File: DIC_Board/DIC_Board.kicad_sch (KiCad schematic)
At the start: 0 parts

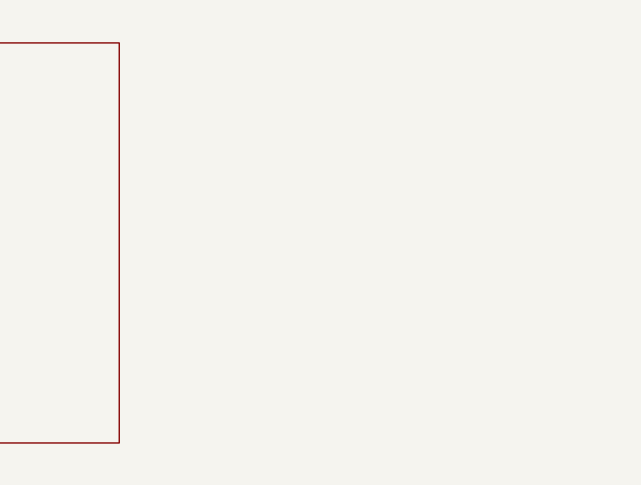
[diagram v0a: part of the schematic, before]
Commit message: Add MCU schematic hierarchy and pin configuration
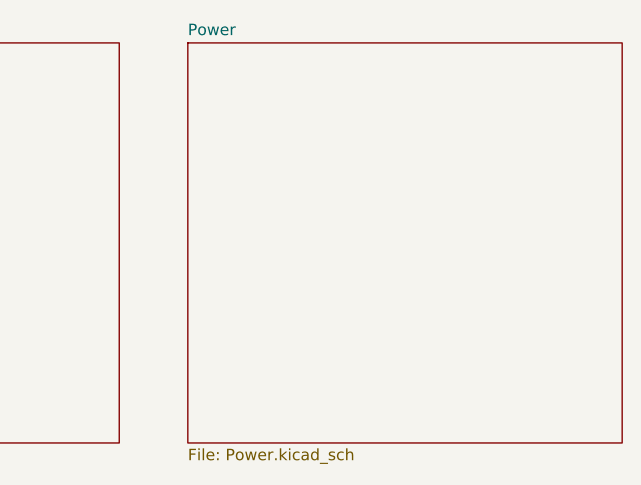
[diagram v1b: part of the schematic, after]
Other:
- added sheet Power (Power.kicad_sch)
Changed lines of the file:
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@@
 	(paper "A4")
+	(sheet
+		(at 91.44 26.67)
+		(size 48.26 44.45)
+		(exclude_from_sim no)
+		(in_bom yes)
+		(on_board yes)
+		(dnp no)
+		(fields_autoplaced yes)
+		(stroke
+			(width 0.1524)
+			(type solid)
+		)
+		(fill
+			(color 0 0 0 0)
+		)
+		(property "Sheetname" "Power"
+			(at 91.44 25.9584 0)
+			(show_name no)
+			(do_not_autoplace no)
+			(effects
+				(font
+					(size 1.27 1.27)
+				)
+				(justify left bottom)
+			)
+		)
+		(property "Sheetfile" "Power.kicad_sch"
+			(at 91.44 71.7046 0)
+			(show_name no)
+			(do_not_autoplace no)
+			(effects
+				(font
+					(size 1.27 1.27)
+				)
+				(justify left top)
+			)
+		)
+		(instances
+			(project "DIC_Board"
+				(path "/bb0ef0df-c181-443a-843c-695cd2e0efee"
+					(page "3")
+				)
+			)
+		)
+	)
 	(sheet
 		(at 35.56 26.67)

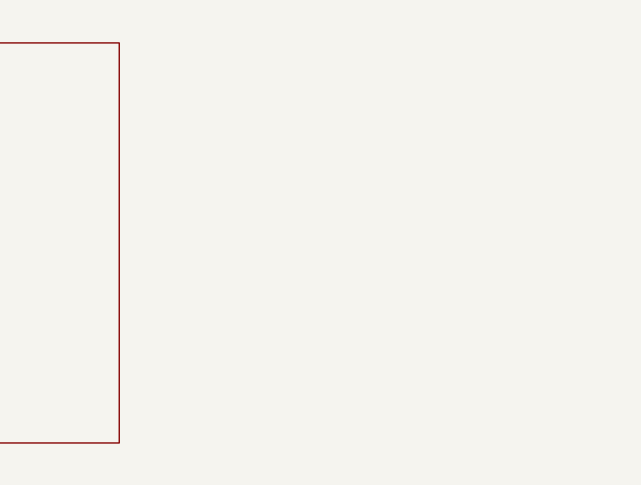
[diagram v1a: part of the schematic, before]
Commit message: added valve control sheet
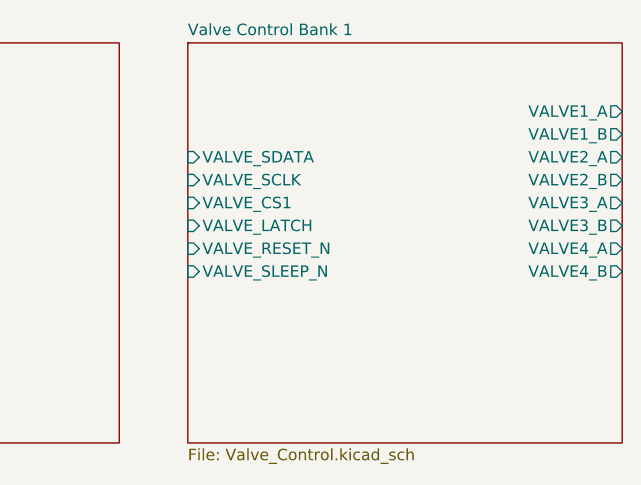
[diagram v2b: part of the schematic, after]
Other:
- added sheet Valve Control Bank 1 (Valve_Control.kicad_sch)
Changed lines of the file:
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@@
 	(paper "A4")
+	(sheet
+		(at 147.32 26.67)
+		(size 48.26 44.45)
+		(exclude_from_sim no)
+		(in_bom yes)
+		(on_board yes)
+		(dnp no)
+		(fields_autoplaced yes)
+		(stroke
+			(width 0.1524)
+			(type solid)
+		)
+		(fill
+			(color 0 0 0 0)
+		)
+		(property "Sheetname" "Valve Control Bank 1"
+			(at 147.32 25.9584 0)
+			(show_name no)
+			(do_not_autoplace no)
+			(effects
+				(font
+					(size 1.27 1.27)
+				)
+				(justify left bottom)
+			)
+		)
+		(property "Sheetfile" "Valve_Control.kicad_sch"
+			(at 147.32 71.7046 0)
+			(show_name no)
+			(do_not_autoplace no)
+			(effects
+				(font
+					(size 1.27 1.27)
+				)
+				(justify left top)
+			)
+		)
+		(pin "VALVE_SDATA" input
+			(at 147.32 39.37 180)
+			(effects
+				(font
+					(size 1.27 1.27)
+				)
+				(justify right)
+			)
+		)
+		(pin "VALVE_SCLK" input
+			(at 147.32 41.91 180)
+			(effects
+				(font
+					(size 1.27 1.27)
+				)
+				(justify right)
+			)
+		)
+		(pin "VALVE_CS1" input
+			(at 147.32 44.45 180)
+			(effects
+				(font
+					(size 1.27 1.27)
+				)
+				(justify right)
+			)
+		)
+		(pin "VALVE_LATCH" input
+			(at 147.32 46.99 180)
+			(effects
+				(font
+					(size 1.27 1.27)
+				)
+				(justify right)
+			)
+		)
+		(pin "VALVE_RESET_N" input
+			(at 147.32 49.53 180)
+			(effects
+				(font
+					(size 1.27 1.27)
+				)
+				(justify right)
+			)
+		)
+		(pin "VALVE_SLEEP_N" input
+			(at 147.32 52.07 180)
+			(effects
+				(font
+					(size 1.27 1.27)
+				)
+				(justify right)
+			)
+		)
+		(pin "VALVE1_A" output
+			(at 195.58 34.29 0)
+			(effects
+				(font
+					(size 1.27 1.27)
+				)
+				(justify left)
+			)
+		)
+		(pin "VALVE1_B" output
+			(at 195.58 36.83 0)
+			(effects
+				(font
+					(size 1.27 1.27)
+				)
+				(justify left)
+			)
+		)
+		(pin "VALVE2_A" output
+			(at 195.58 39.37 0)
+			(effects
+				(font
+					(size 1.27 1.27)
+				)
+				(justify left)
+			)
+		)
+		(pin "VALVE2_B" output
+			(at 195.58 41.91 0)
+			(effects
+				(font
+					(size 1.27 1.27)
+				)
+				(justify left)
+			)
+		)
+		(pin "VALVE3_A" output
+			(at 195.58 44.45 0)
+			(effects
+				(font
+					(size 1.27 1.27)
+				)
+				(justify left)
+			)
+		)
+		(pin "VALVE3_B" output
+			(at 195.58 46.99 0)
+			(effects
+				(font
+					(size 1.27 1.27)
+				)
+				(justify left)
+			)
+		)
+		(pin "VALVE4_A" output
+			(at 195.58 49.53 0)
+			(effects
+				(font
+					(size 1.27 1.27)
+				)
+				(justify left)
+			)
+		)
+		(pin "VALVE4_B" output
+			(at 195.58 52.07 0)
+			(effects
+				(font
+					(size 1.27 1.27)
+				)
+				(justify left)
+			)
+		)
+		(instances
+			(project "DIC_Board"
+				(path "/bb0ef0df-c181-443a-843c-695cd2e0efee"
+					(page "4")
+				)
+			)
+		)
+	)
 	(sheet
 		(at 91.44 26.67)
@@
 		)
 	)
-	(embedded_fonts no)
 )

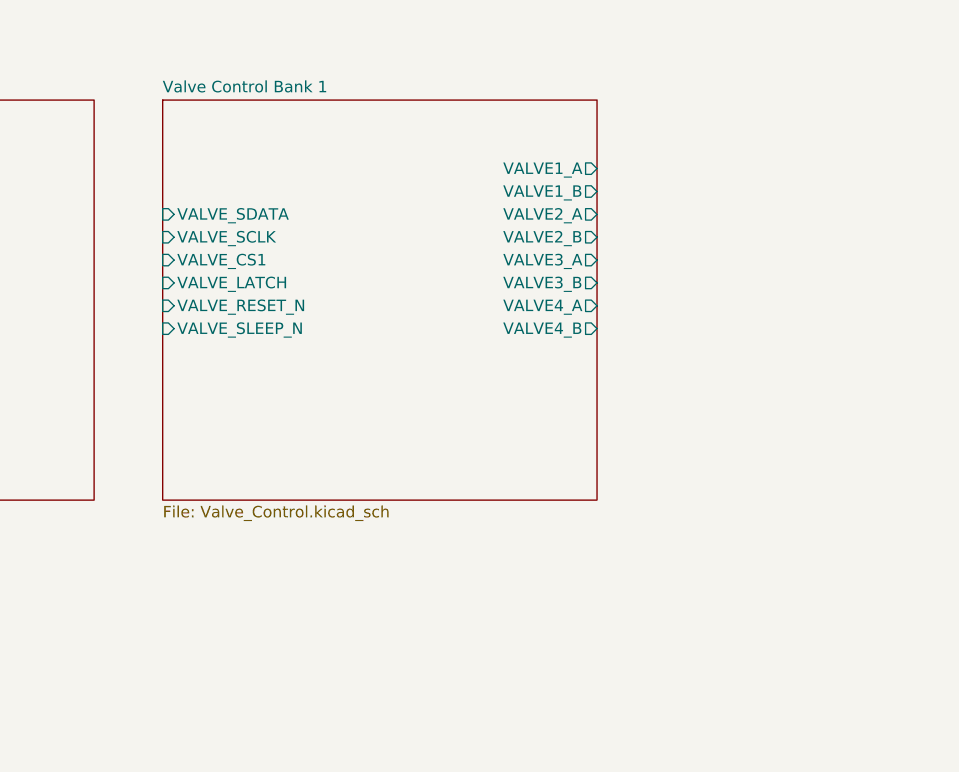
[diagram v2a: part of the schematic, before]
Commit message: added valve control banks.
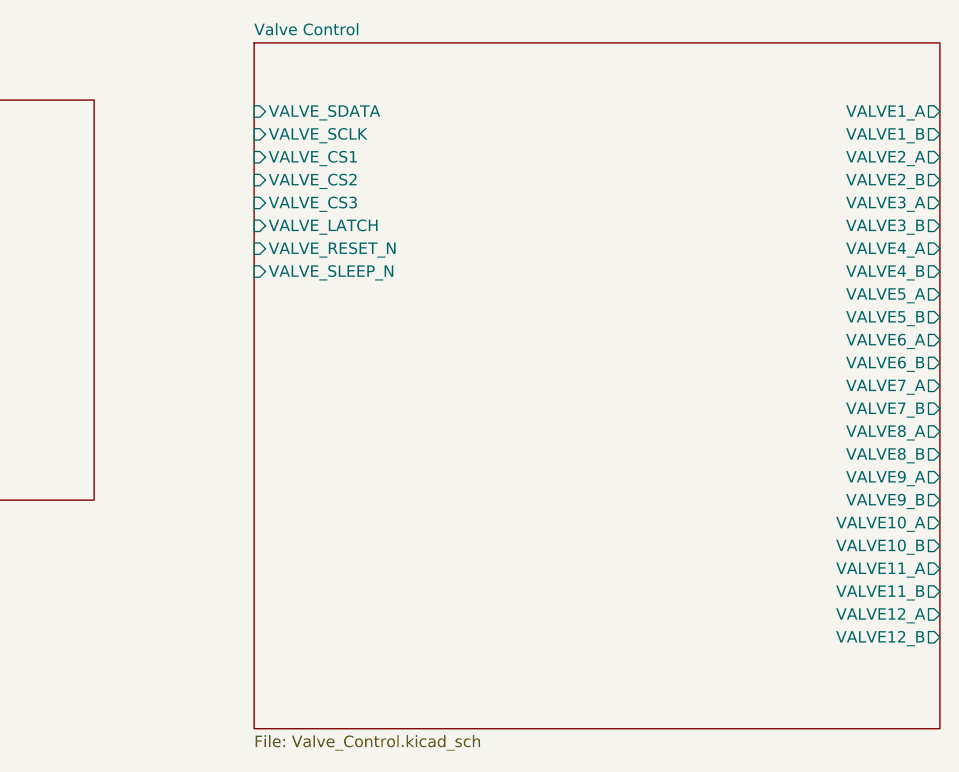
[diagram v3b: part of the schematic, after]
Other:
- sheet Valve Control Bank 1 renamed Valve Control
- sheet Valve Control ports: added VALVE10_A, VALVE10_B, VALVE11_A, VALVE11_B, VALVE12_A, VALVE12_B, VALVE5_A, VALVE5_B, VALVE6_A, VALVE6_B, VALVE7_A, VALVE7_B, VALVE8_A, VALVE8_B, VALVE9_A, VALVE9_B, VALVE_CS2, VALVE_CS3; removed none
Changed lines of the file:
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@@
 	(paper "A4")
 	(sheet
-		(at 147.32 26.67)
-		(size 48.26 44.45)
+		(at 157.48 20.32)
+		(size 76.2 76.2)
 		(exclude_from_sim no)
 		(in_bom yes)
@@
 			(color 0 0 0 0)
 		)
-		(property "Sheetname" "Valve Control Bank 1"
-			(at 147.32 25.9584 0)
+		(property "Sheetname" "Valve Control"
+			(at 157.48 19.6084 0)
 			(show_name no)
 			(do_not_autoplace no)
@@
 		)
 		(property "Sheetfile" "Valve_Control.kicad_sch"
-			(at 147.32 71.7046 0)
+			(at 157.48 97.2316 0)
 			(show_name no)
 			(do_not_autoplace no)
@@
 		)
 		(pin "VALVE_SDATA" input
-			(at 147.32 39.37 180)
+			(at 157.48 27.94 180)
 			(effects
 				(font
@@
 		)
 		(pin "VALVE_SCLK" input
-			(at 147.32 41.91 180)
+			(at 157.48 30.48 180)
 			(effects
 				(font
@@
 		)
 		(pin "VALVE_CS1" input
-			(at 147.32 44.45 180)
+			(at 157.48 33.02 180)
+			(effects
+				(font
+					(size 1.27 1.27)
+				)
+				(justify right)
+			)
+		)
+		(pin "VALVE_CS2" input
+			(at 157.48 35.56 180)
+			(effects
+				(font
+					(size 1.27 1.27)
+				)
+				(justify right)
+			)
+		)
+		(pin "VALVE_CS3" input
+			(at 157.48 38.1 180)
 			(effects
 				(font
@@
 		)
 		(pin "VALVE_LATCH" input
-			(at 147.32 46.99 180)
+			(at 157.48 40.64 180)
 			(effects
 				(font
@@
 		)
 		(pin "VALVE_RESET_N" input
-			(at 147.32 49.53 180)
+			(at 157.48 43.18 180)
 			(effects
 				(font
@@
 		)
 		(pin "VALVE_SLEEP_N" input
-			(at 147.32 52.07 180)
+			(at 157.48 45.72 180)
 			(effects
 				(font
@@
 		)
 		(pin "VALVE1_A" output
-			(at 195.58 34.29 0)
+			(at 233.68 27.94 0)
 			(effects
 				(font
@@
 		)
 		(pin "VALVE1_B" output
-			(at 195.58 36.83 0)
+			(at 233.68 30.48 0)
 			(effects
 				(font
@@
 		)
 		(pin "VALVE2_A" output
-			(at 195.58 39.37 0)
+			(at 233.68 33.02 0)
 			(effects
 				(font
@@
 		)
 		(pin "VALVE2_B" output
-			(at 195.58 41.91 0)
+			(at 233.68 35.56 0)
 			(effects
 				(font
@@
 		)
 		(pin "VALVE3_A" output
-			(at 195.58 44.45 0)
+			(at 233.68 38.1 0)
 			(effects
 				(font
@@
 		)
 		(pin "VALVE3_B" output
-			(at 195.58 46.99 0)
+			(at 233.68 40.64 0)
 			(effects
 				(font
@@
 		)
 		(pin "VALVE4_A" output
-			(at 195.58 49.53 0)
+			(at 233.68 43.18 0)
 			(effects
 				(font
@@
 		)
 		(pin "VALVE4_B" output
-			(at 195.58 52.07 0)
+			(at 233.68 45.72 0)
+			(effects
+				(font
+					(size 1.27 1.27)
+				)
+				(justify left)
+			)
+		)
+		(pin "VALVE5_A" output
+			(at 233.68 48.26 0)
+			(effects
+				(font
+					(size 1.27 1.27)
+				)
+				(justify left)
+			)
+		)
+		(pin "VALVE5_B" output
+			(at 233.68 50.8 0)
+			(effects
+				(font
+					(size 1.27 1.27)
+				)
+				(justify left)
+			)
+		)
+		(pin "VALVE6_A" output
+			(at 233.68 53.34 0)
+			(effects
+				(font
+					(size 1.27 1.27)
+				)
+				(justify left)
+			)
+		)
+		(pin "VALVE6_B" output
+			(at 233.68 55.88 0)
+			(effects
+				(font
+					(size 1.27 1.27)
+				)
+				(justify left)
+			)
+		)
+		(pin "VALVE7_A" output
+			(at 233.68 58.42 0)
+			(effects
+				(font
+					(size 1.27 1.27)
+				)
+				(justify left)
+			)
+		)
+		(pin "VALVE7_B" output
+			(at 233.68 60.96 0)
+			(effects
+				(font
+					(size 1.27 1.27)
+				)
+				(justify left)
+			)
+		)
+		(pin "VALVE8_A" output
+			(at 233.68 63.5 0)
+			(effects
+				(font
+					(size 1.27 1.27)
+				)
+				(justify left)
+			)
+		)
+		(pin "VALVE8_B" output
+			(at 233.68 66.04 0)
+			(effects
+				(font
+					(size 1.27 1.27)
+				)
+				(justify left)
+			)
+		)
+		(pin "VALVE9_A" output
+			(at 233.68 68.58 0)
+			(effects
+				(font
+					(size 1.27 1.27)
+				)
+				(justify left)
+			)
+		)
+		(pin "VALVE9_B" output
+			(at 233.68 71.12 0)
+			(effects
+				(font
+					(size 1.27 1.27)
+				)
+				(justify left)
+			)
+		)
+		(pin "VALVE10_A" output
+			(at 233.68 73.66 0)
+			(effects
+				(font
+					(size 1.27 1.27)
+				)
+				(justify left)
+			)
+		)
+		(pin "VALVE10_B" output
+			(at 233.68 76.2 0)
+			(effects
+				(font
+					(size 1.27 1.27)
+				)
+				(justify left)
+			)
+		)
+		(pin "VALVE11_A" output
+			(at 233.68 78.74 0)
+			(effects
+				(font
+					(size 1.27 1.27)
+				)
+				(justify left)
+			)
+		)
+		(pin "VALVE11_B" output
+			(at 233.68 81.28 0)
+			(effects
+				(font
+					(size 1.27 1.27)
+				)
+				(justify left)
+			)
+		)
+		(pin "VALVE12_A" output
+			(at 233.68 83.82 0)
+			(effects
+				(font
+					(size 1.27 1.27)
+				)
+				(justify left)
+			)
+		)
+		(pin "VALVE12_B" output
+			(at 233.68 86.36 0)
 			(effects
 				(font
@@
 		)
 	)
+	(embedded_fonts no)
 )

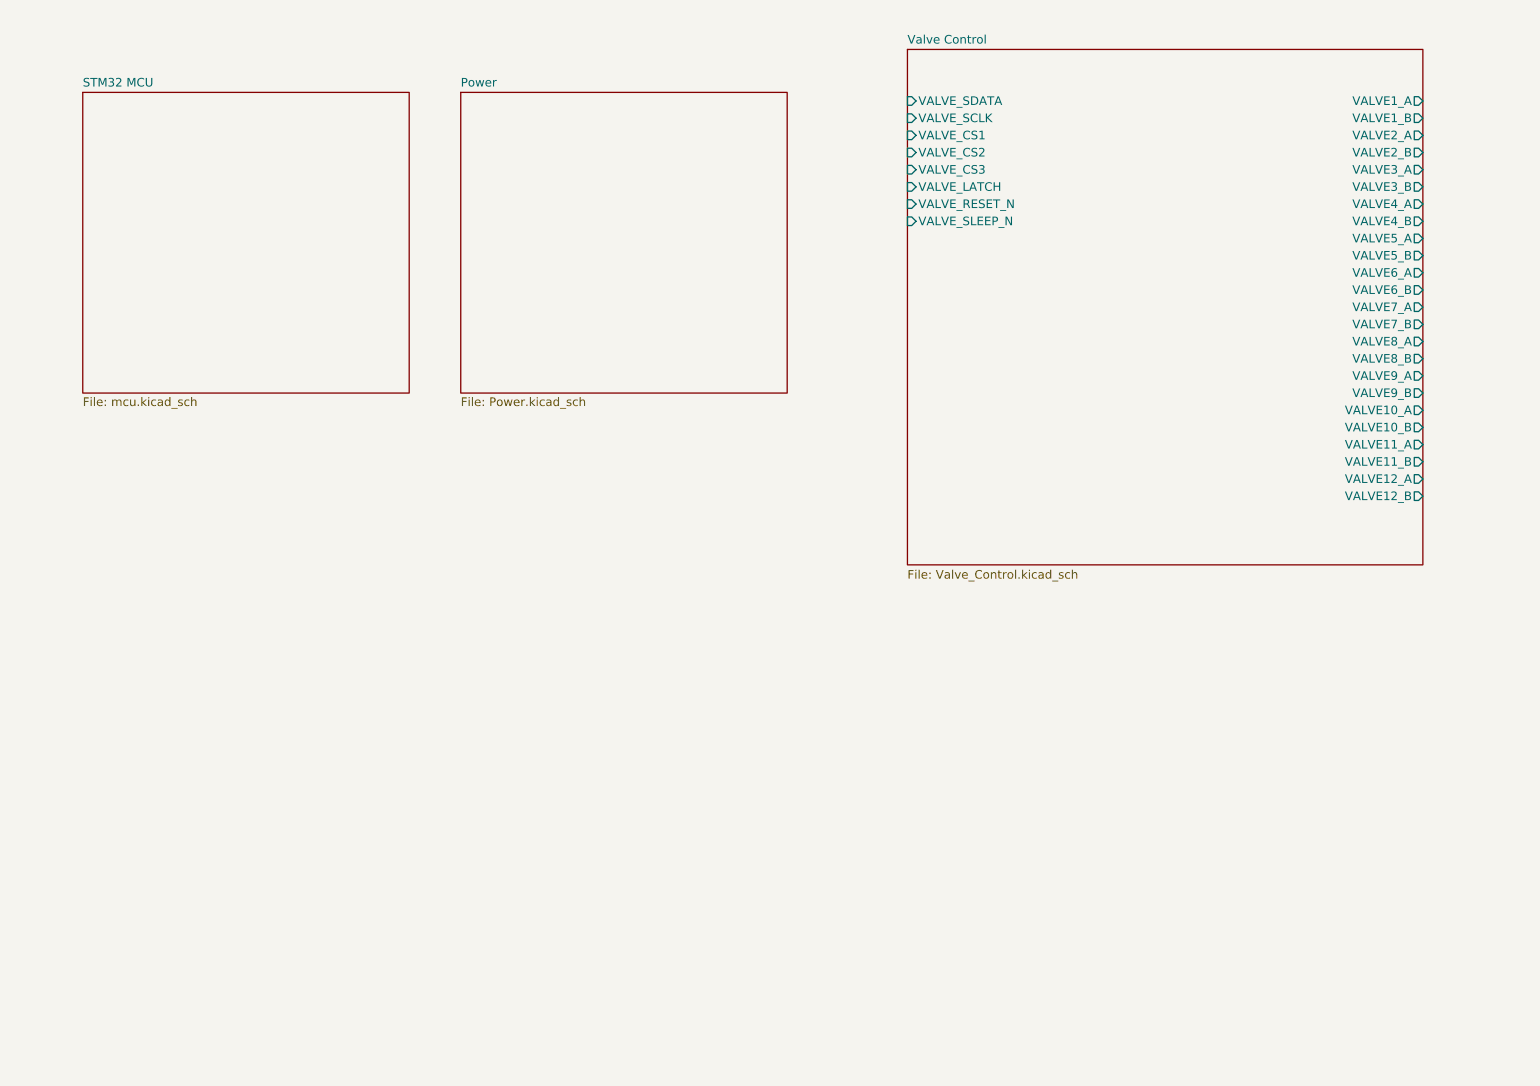
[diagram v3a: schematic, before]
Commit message: Added Sheets for pumps and sensors
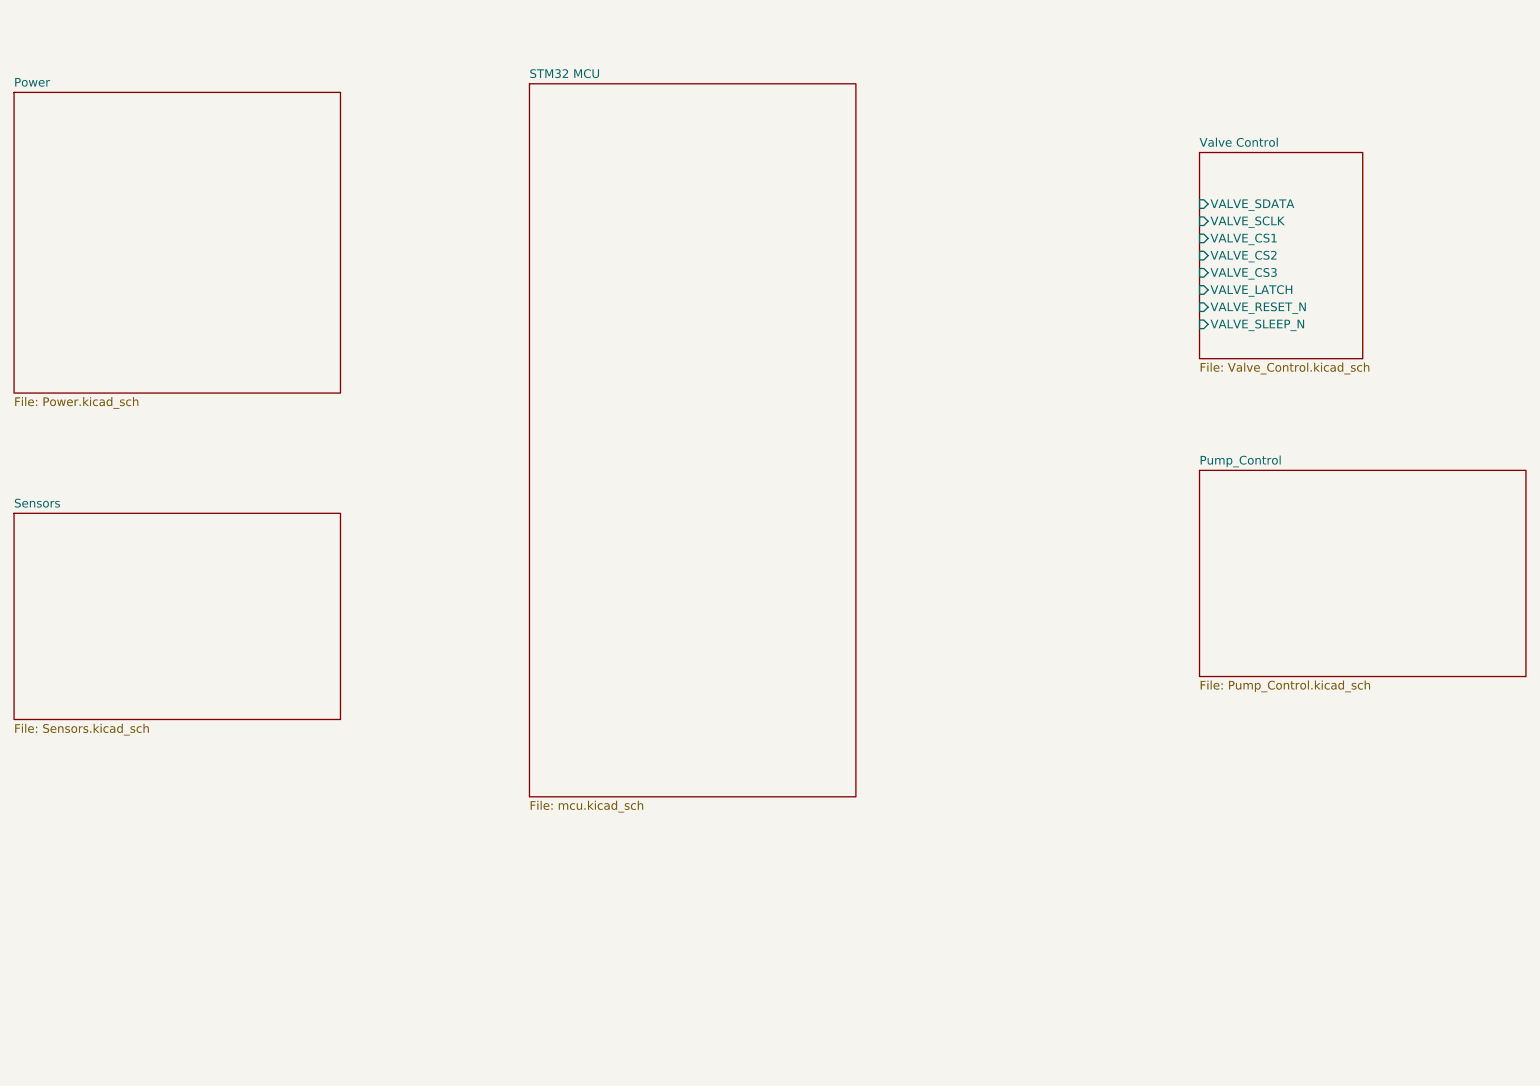
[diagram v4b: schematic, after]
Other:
- added sheet Pump_Control (Pump_Control.kicad_sch)
- added sheet Sensors (Sensors.kicad_sch)
- sheet Valve Control ports: added none; removed VALVE10_A, VALVE10_B, VALVE11_A, VALVE11_B, VALVE12_A, VALVE12_B, VALVE1_A, VALVE1_B, VALVE2_A, VALVE2_B, VALVE3_A, VALVE3_B, VALVE4_A, VALVE4_B, VALVE5_A, VALVE5_B, VALVE6_A, VALVE6_B, VALVE7_A, VALVE7_B, VALVE8_A, VALVE8_B, VALVE9_A, VALVE9_B
